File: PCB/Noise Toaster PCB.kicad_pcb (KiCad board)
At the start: 2 copper layers, 132.1 x 68.6 mm, 137 parts, among them J2 Power, J3 AREG, J4 LFO, J5 VCO, J6 VCO, J7 VCLPF, J8 VCA, J9 Amp, Q1 2N5457, Q10 2N3906, Q2 2N3904, Q3 2N3904, Q4 2N3904, Q5 2N3904, Q6 2N3904, Q7 2N5457, Q8 2N5457, Q9 2N5457, U1 LM324, U2 LM324, U3 LM386, X4 WNS

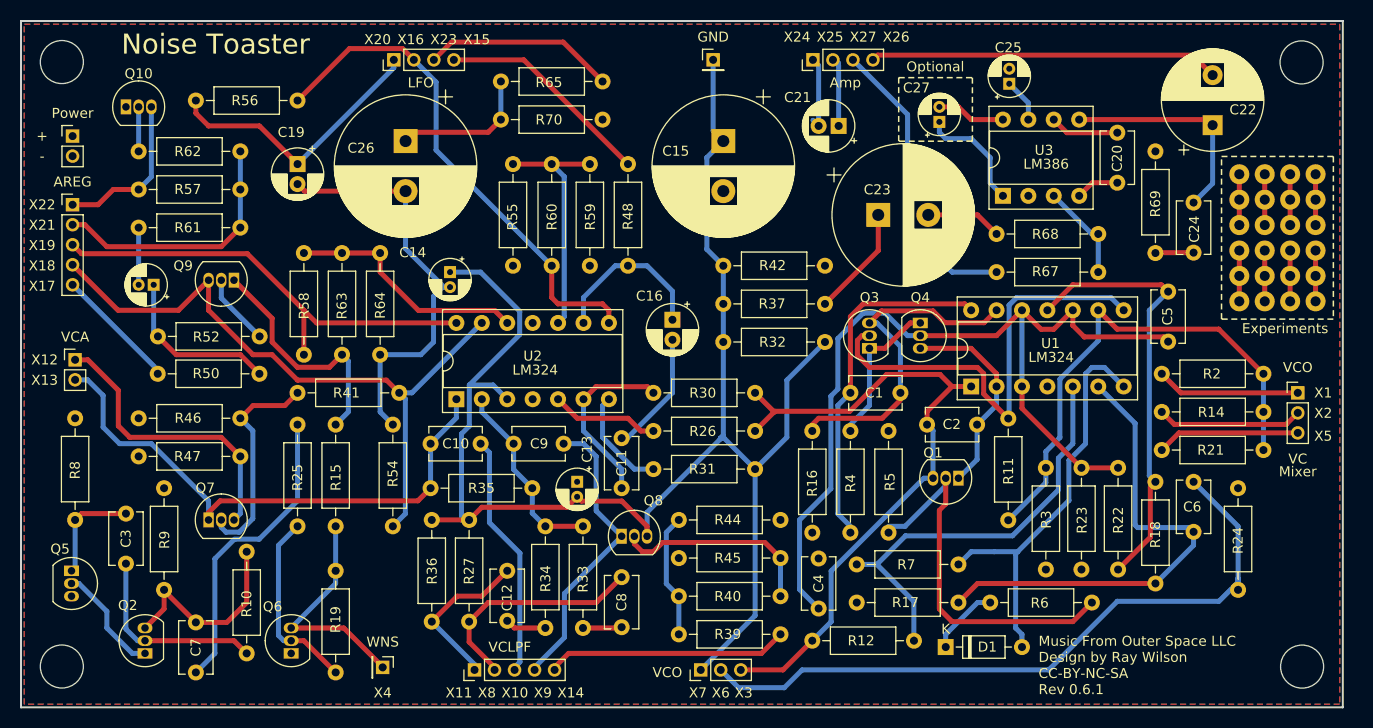
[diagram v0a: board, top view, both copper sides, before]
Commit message: Update to Kicad 10
Changes: Moved some traces around to allow more ground fill
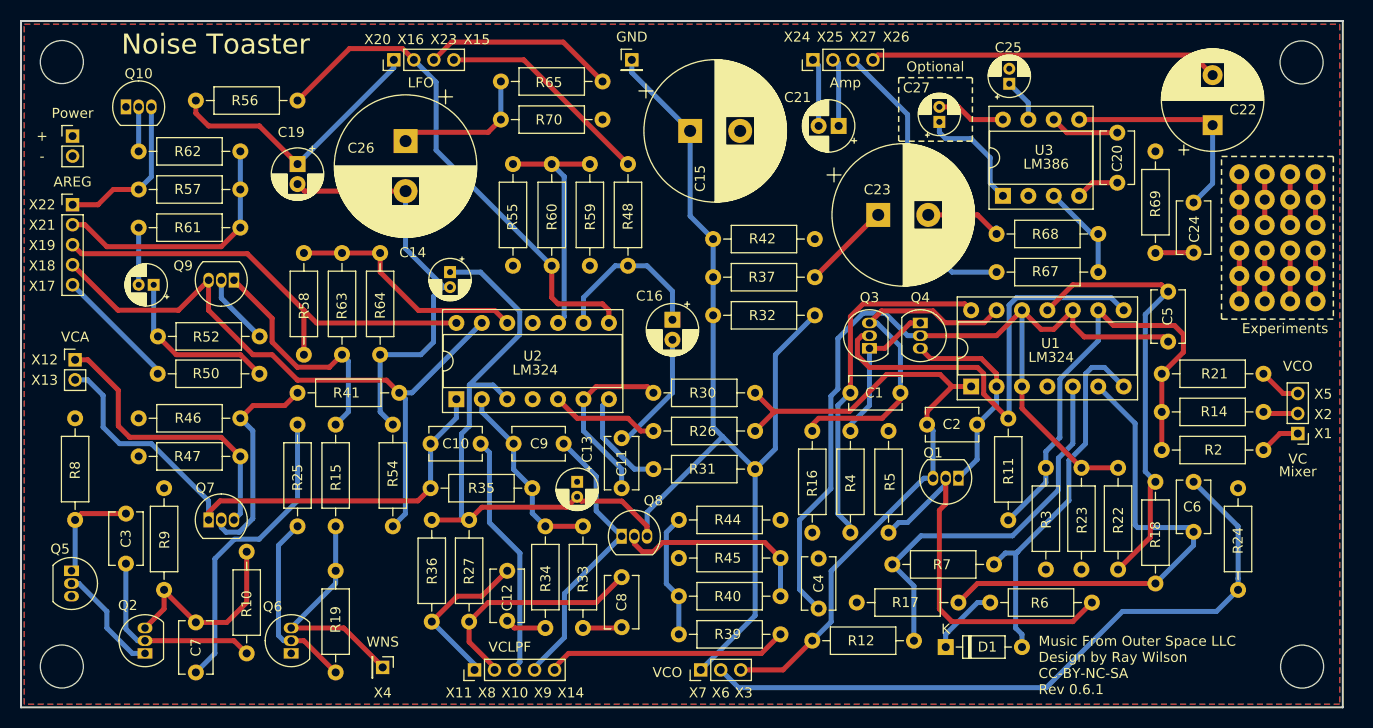
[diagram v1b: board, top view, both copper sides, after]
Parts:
- moved R2 12.7 mm to (189.3, 118.1), turned to 0 degrees
- moved R21 12.7 mm to (189.3, 110.5), turned to 0 degrees
- moved R14 10.2 mm to (189.3, 114.3), turned to 0 degrees
- moved GND1 8.13 mm to (136.3, 79.1)
- moved J5 4.06 mm to (202.8, 116.5), turned to 180 degrees
- moved R7 3.56 mm to (162.3, 129.6)
- moved C15 3.47 mm to (142.1, 86.2), turned to 0 degrees
- moved R32 2.85 mm to (144.4, 104.7)
- moved R37 2.85 mm to (154.6, 100.9)
- moved R42 2.85 mm to (144.4, 97.1)
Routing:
- net /Front Panel/X2: track 14.6 -> 3.27 mm
- net /Front Panel/X1: track 14.4 -> 4.11 mm
- net /Front Panel/X5: track 14.3 -> 4.24 mm
- net Net-(U1C--): track 51.5 -> 46.7 mm
- net Net-(U1B-+): track 43.3 -> 39.1 mm
- net B+: track 42.1 -> 38.5 mm
- net Net-(D1-A): track 41.8 -> 38.2 mm
- net GND: track 158.2 -> 160.9 mm
- net Net-(C26-Pad1): track 14.2 -> 13.0 mm
- net /Front Panel/X9: track 29.5 -> 28.4 mm
- net /Audio Amplifier/X24: track 7.65 -> 6.84 mm
- net B-: track 129.5 -> 128.7 mm
- net Net-(C22-Pad1): track 22.1 -> 21.3 mm
- net /Front Panel/X6: track 69.8 -> 69.1 mm

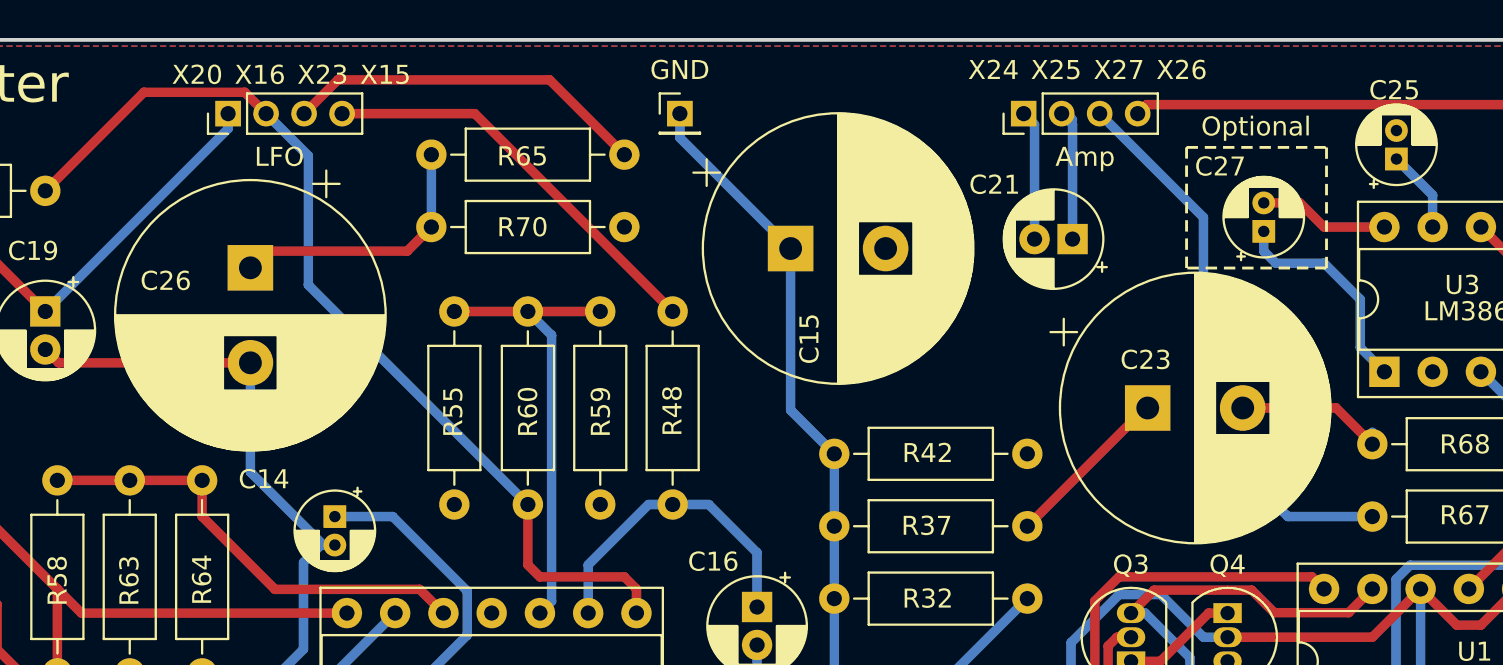
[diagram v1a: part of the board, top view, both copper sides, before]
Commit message: Changed Footprint
470uF/50V Caps are 10mm not 14
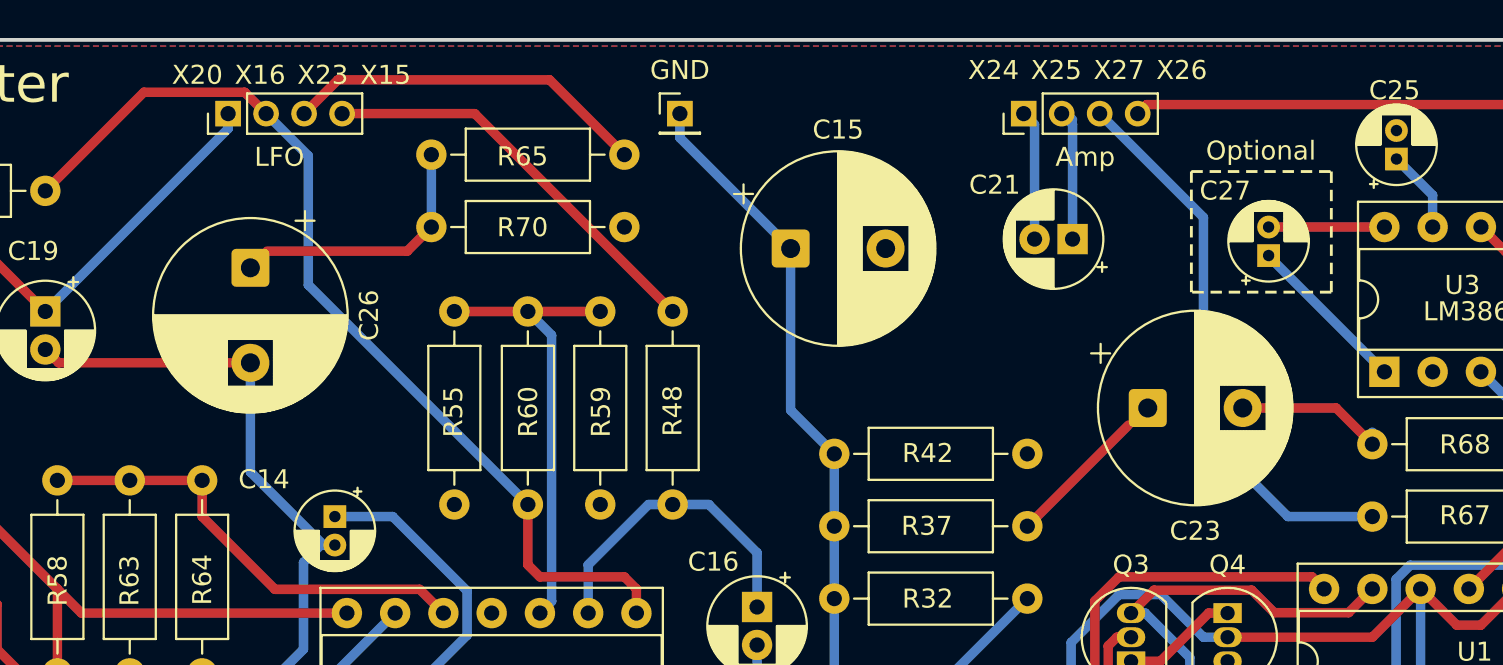
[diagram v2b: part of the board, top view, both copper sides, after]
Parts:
- C15, C23, C26: footprint Capacitor_THT:CP_Radial_D14.0mm_P5.00mm -> Capacitor_THT:CP_Radial_D10.0mm_P5.00mm
- moved C27 1.30 mm to (167.3, 86.6)
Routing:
- net Net-(C27-Pad1): track 11.5 -> 8.65 mm
- net Net-(C27-Pad2): track 6.88 -> 6.10 mm

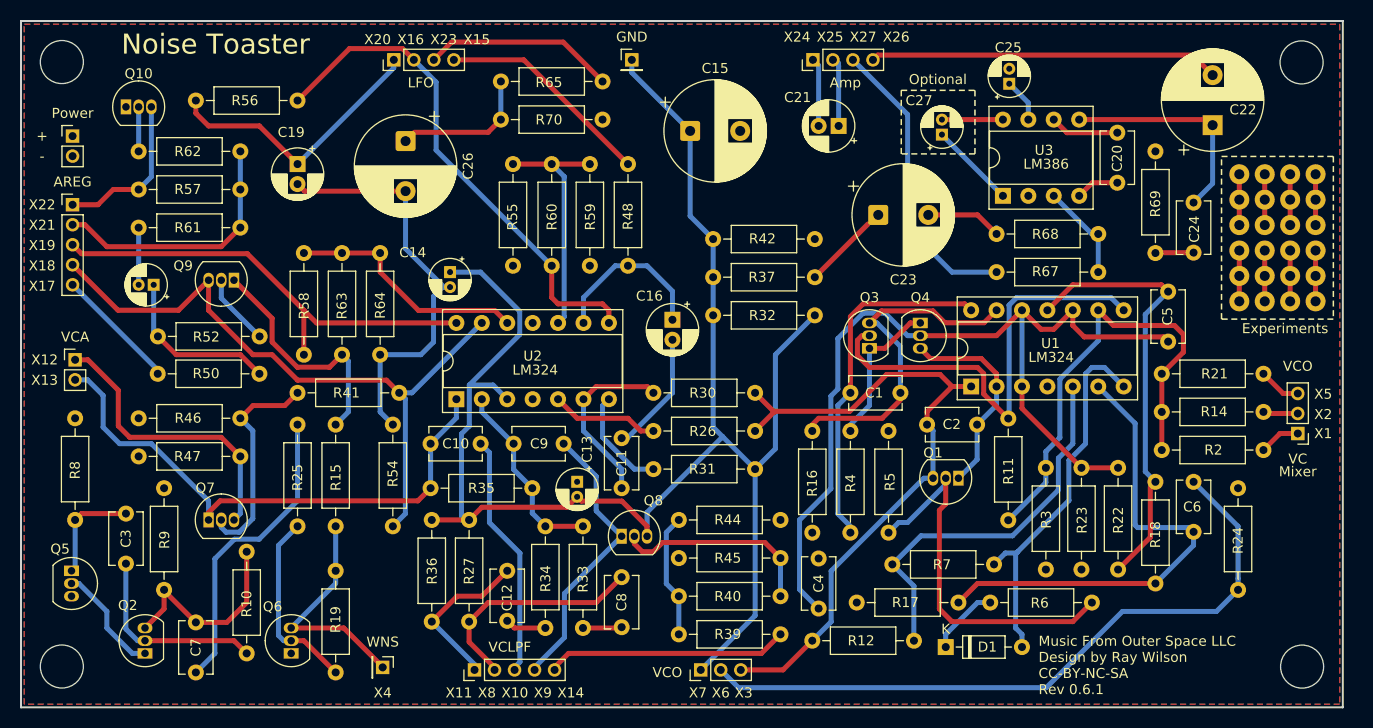
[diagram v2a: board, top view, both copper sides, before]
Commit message: Change M4 to M3 Holes
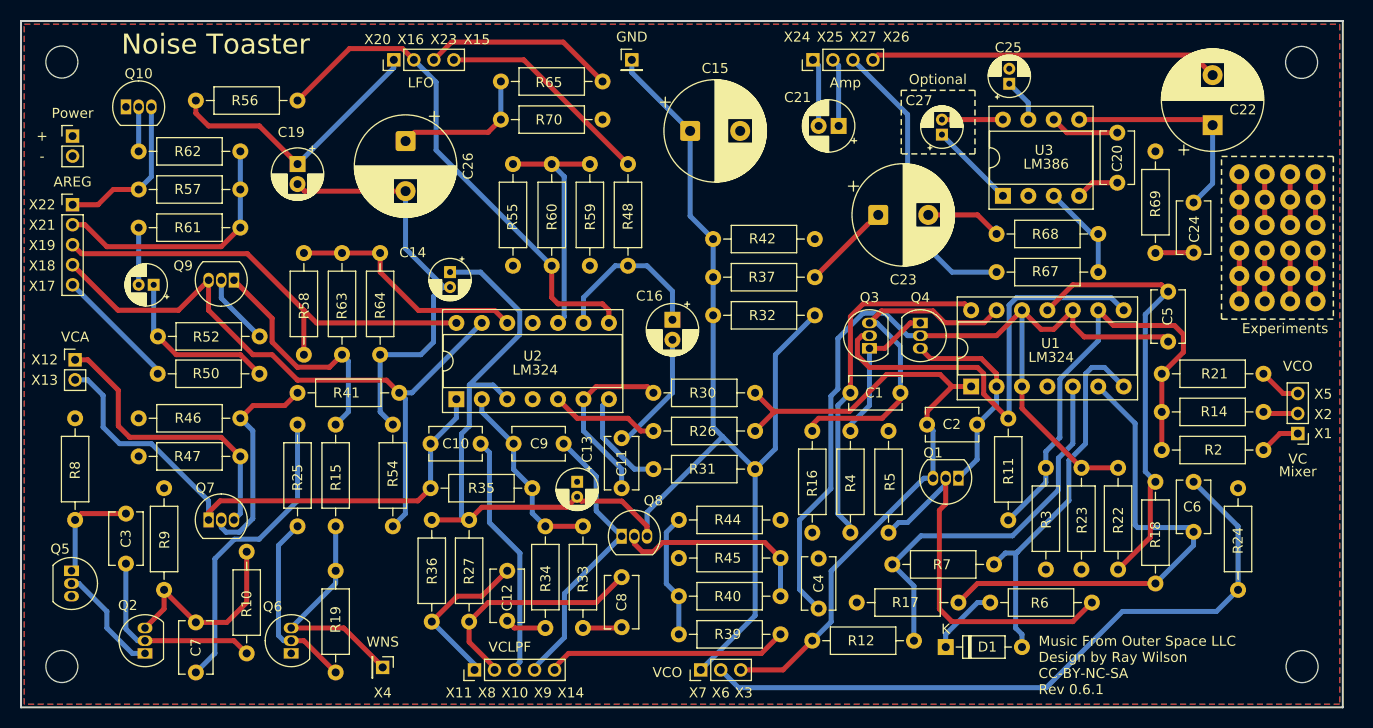
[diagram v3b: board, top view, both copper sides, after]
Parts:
- REF** (x4): value MountingHole_4.3mm_M4_DIN965 -> MountingHole_3.2mm_M3_DIN965; footprint MountingHole:MountingHole_4.3mm_M4_DIN965 -> MountingHole:MountingHole_3.2mm_M3_DIN965
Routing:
- net /Audio Amplifier/X25: track 7.65 -> 6.84 mm
